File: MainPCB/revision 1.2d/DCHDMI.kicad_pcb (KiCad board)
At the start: 2 copper layers, 66.6 x 51.3 mm, 235 parts, among them CON1 3-1775333-2, CON2 2001-1-2-21-00-BK, CON3 CONN_01X06, CON4 CONN_01X03, U1 MCP1826S-1202E/DB, U2 MIC5219-2.5YM5-TR, U3 LP5907MFX-1.8/NOPB, U4 ADV7513, U5 664G-03LF, U6 10CL025, U7 MX25L1606EM1I-12G, U8 ESP-12E

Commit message: Added 1.2d
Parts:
- removed the ? at (133.8, 117.0)
- removed the ? at (133.8, 115.2)
- added ?: , pads:via-3mm, F.Cu at (140.9, 106.2)
- added ?: , pads:via-3mm, F.Cu at (148.6, 89.3)
- added ?: , pads:via-3mm, F.Cu at (186.4, 91.8)
- added ?: , pads:via-3mm, F.Cu at (186.4, 90.2)
- added ?: , pads:via-3mm, F.Cu at (186.4, 88.6)
- added ?: , pads:via-3mm, F.Cu at (169.1, 96.2)
- added ?: , pads:via-3mm, F.Cu at (169.1, 95.0)
- added ?: , pads:via-3mm, F.Cu at (169.2, 91.9)
- added ?: , pads:via-3mm, F.Cu at (169.1, 93.8)
- added ?: , pads:via-3mm, F.Cu at (158.2, 91.9)
- added ?: , pads:via-3mm, F.Cu at (160.4, 91.9)
- added ?: , pads:via-3mm, F.Cu at (136.0, 116.0)
- added ?: , pads:via-3mm, F.Cu at (155.8, 101.0)
- added ?: , pads:.6Cast, F.Cu at (168.3, 109.4)
- added ?: , pads:via-3mm, F.Cu at (153.2, 98.8)
- added ?: , pads:via-3mm, F.Cu at (154.2, 118.7)
- added ?: , pads:via-3mm, F.Cu at (158.4, 123.8)
- added ?: , pads:via-3mm, F.Cu at (161.4, 112.1)
- added ?: , pads:via-3mm, F.Cu at (160.2, 112.2)
- added ?: , pads:via-3mm, F.Cu at (163.4, 121.6)
- added ?: , pads:via-3mm, F.Cu at (160.8, 121.7)
- added ?: , pads:via-3mm, F.Cu at (158.7, 121.7)
- added ?: , pads:via-3mm, F.Cu at (146.2, 121.7)
- added ?: , pads:via-3mm, F.Cu at (135.3, 114.9)
- added ?: , pads:via-3mm, F.Cu at (148.1, 111.0)
- added ?: , pads:via-3mm, F.Cu at (149.6, 111.0)
- added ?: , pads:via-3mm, F.Cu at (152.9, 118.7)
- added ?: , pads:.6Cast, F.Cu at (184.7, 123.4)
- added ?: , pads:.6Cast, F.Cu at (184.7, 121.4)
- added ?: , pads:.6Cast, F.Cu at (184.7, 119.4)
- added ?: , pads:.6Cast, F.Cu at (184.7, 117.4)
- added ?: , pads:.6Cast, F.Cu at (184.7, 115.4)
- added ?: , pads:.6Cast, F.Cu at (184.7, 113.4)
- added ?: , pads:.6Cast, F.Cu at (184.7, 111.4)
- added ?: , pads:via-3mm, F.Cu at (141.6, 107.8)
- added ?: , pads:.6Cast, F.Cu at (184.7, 109.4)
- added ?: , pads:.6Cast, F.Cu at (168.3, 123.4)
- added ?: , pads:.6Cast, F.Cu at (168.3, 121.4)
- added ?: , pads:.6Cast, F.Cu at (168.3, 119.4)
- added ?: , pads:.6Cast, F.Cu at (168.3, 117.4)
- added ?: , pads:.6Cast, F.Cu at (168.3, 115.4)
- added ?: , pads:.6Cast, F.Cu at (168.3, 113.4)
- added ?: , pads:.6Cast, F.Cu at (168.3, 111.4)
- added ?: , pads:via-3mm, F.Cu at (186.4, 101.2)
- added ?: , pads:via-3mm, F.Cu at (184.3, 101.2)
- added ?: , pads:via-3mm, F.Cu at (141.9, 111.5)
- added ?: , pads:via-3mm, F.Cu at (184.6, 103.5)
- added ?: , pads:via-3mm, F.Cu at (144.2, 111.0)
- added ?: , pads:via-3mm, F.Cu at (144.6, 89.5)
- added ?: , pads:via-3mm, F.Cu at (146.8, 87.0)
- added ?: , pads:via-3mm, F.Cu at (148.7, 87.0)
- added C41: 47p, Capacitors_SMD:C_0603_HandSoldering, F.Cu at (185.3, 97.0)
- added C46: 47p, Capacitors_SMD:C_0603_HandSoldering, F.Cu at (185.3, 98.5)
- added C47: 47p, Capacitors_SMD:C_0603_HandSoldering, F.Cu at (185.3, 100.0)
- added C48: .1u, Capacitors_SMD:C_0603_HandSoldering, F.Cu at (180.9, 105.2)
- added C49: 22u, Capacitors_SMD:C_0603_HandSoldering, F.Cu at (179.4, 105.2)
- added R18: 10K, Capacitors_SMD:C_0603_HandSoldering, F.Cu at (143.9, 120.6)
- added R19: 10K, Capacitors_SMD:C_0603_HandSoldering, F.Cu at (136.6, 120.4)
- added R20: 10K, Capacitors_SMD:C_0603_HandSoldering, F.Cu at (149.9, 118.2)
- added R7: 10K, Capacitors_SMD:C_0603_HandSoldering, F.Cu at (133.8, 116.3)
- ?: renamed from CON3; value CONN_01X06 -> (none)
- ?: renamed from CON4; value CONN_01X03 -> (none)
- JP1: value Jumper_NO_Small -> (none)
- moved C8 0.21 mm to (151.8, 116.8)
- moved C9 0.21 mm to (155.4, 116.8)
- moved ? 0.09 mm to (164.8, 109.8)
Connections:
- U6 pad 145: (no net) -> GND
- U6 pad 21: GND -> /nCE
- U6 pad 9: +3V3 -> Net-(R7-Pad2)
- U8 pad 13: Net-(U8-Pad13) -> /nCE
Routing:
- net GND: track 204.5 -> 272.5 mm, vias 3 -> 2
- net /nCE: track 0.00 -> 34.8 mm, vias 0 -> 1
- net +3V3: track 389.6 -> 406.5 mm, vias 24 -> 27
- net Net-(R7-Pad2): track 0.00 -> 13.6 mm
- net /ABCK: track 67.4 -> 73.5 mm
- net /ADAT: track 66.5 -> 71.9 mm
- net /TDI: track 12.2 -> 16.9 mm
- net /ALRK: track 70.1 -> 73.5 mm
- net /TMS: track 9.11 -> 10.4 mm
- net /TDO: track 8.45 -> 9.34 mm
- net /TCK: track 9.73 -> 10.6 mm
- net /MOSI: track 71.3 -> 71.6 mm, vias 3 -> 2
- net /MISO: track 70.1 -> 70.3 mm, vias 3 -> 2
- net Net-(R14-Pad1): track 49.0 -> 49.2 mm, vias 2 -> 1
- net /DCLK: track 74.4 -> 74.6 mm, vias 3 -> 2
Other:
- board text added: "@chriz2600"
- board text added: "@citrus3000psi"
- board text added: "DCHDMI 1.2d"
- board text added: "P1"
- board text added: "P2"
- board text removed: "@citrus3000psi @chriz2600"
- board text removed: "DCHDMI 1.2a"
- board text removed: "PAD"
- board text removed: "RX"
- board text removed: "TX"

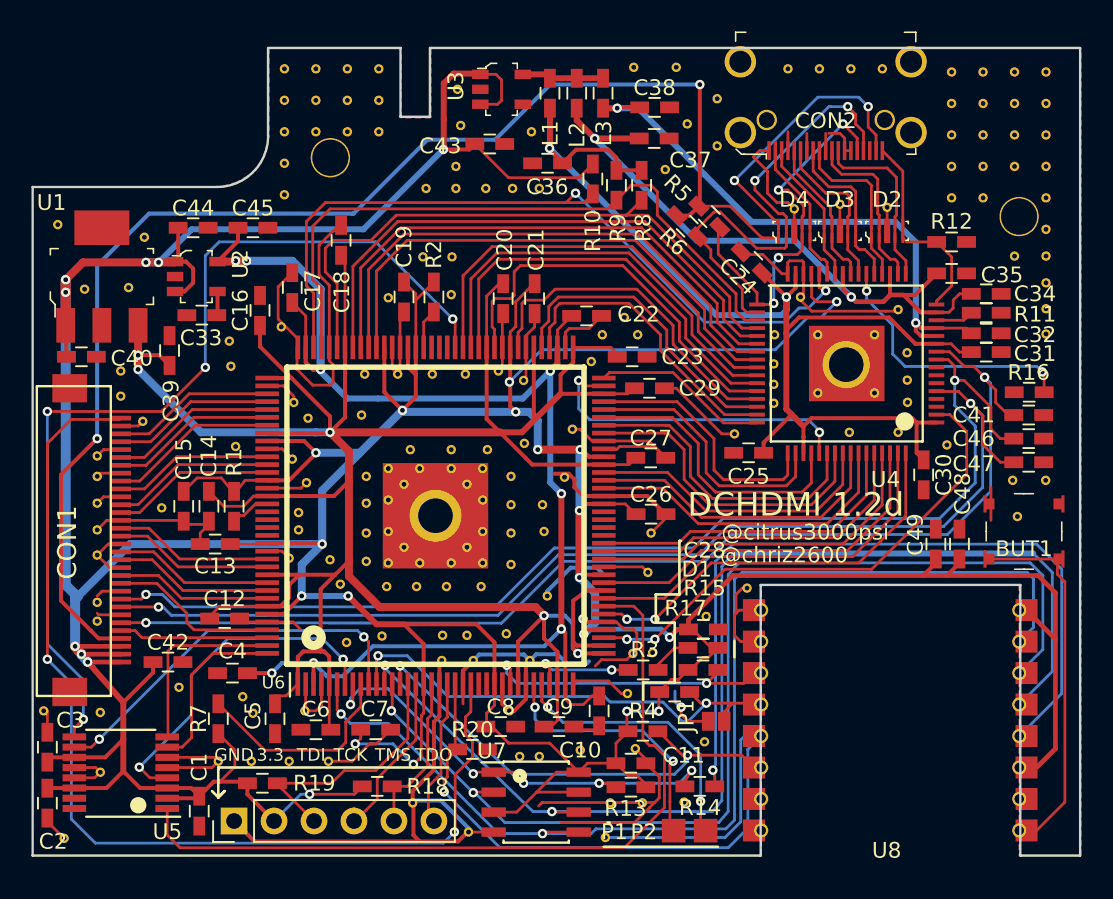
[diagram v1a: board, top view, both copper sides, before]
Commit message: 4 layer version
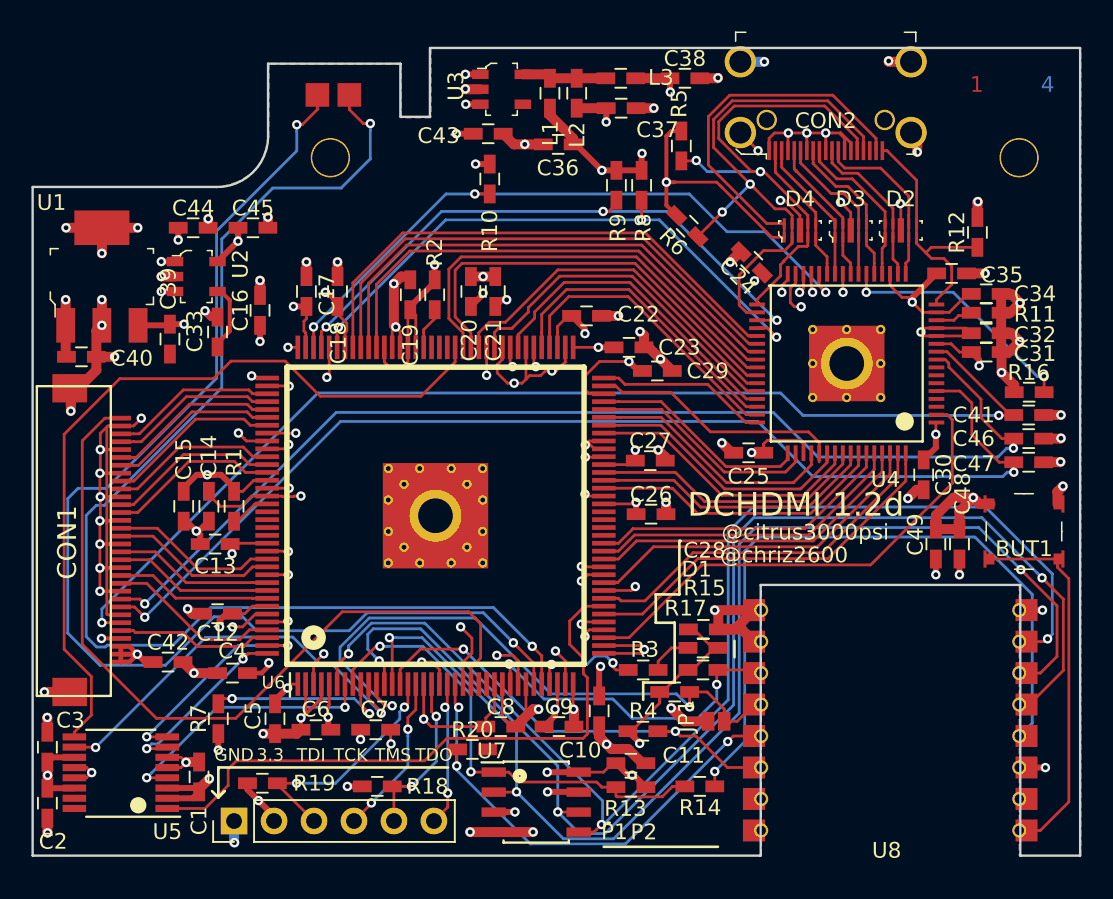
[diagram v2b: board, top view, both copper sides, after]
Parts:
- removed the ? at (140.9, 106.2)
- removed the ? at (148.6, 89.3)
- removed the ? at (124.0, 123.9)
- removed the ? at (139.3, 115.8)
- removed the ? at (170.4, 83.9)
- removed the ? at (173.3, 83.6)
- removed the ? at (176.3, 83.8)
- removed the ? at (167.4, 108.0)
- removed the ? at (166.6, 98.2)
- removed the ? at (170.8, 89.5)
- removed the ? at (180.1, 98.9)
- removed the ? at (131.3, 114.3)
- removed the ? at (186.4, 91.8)
- removed the ? at (126.3, 119.7)
- removed the ? at (145.2, 94.4)
- removed the ? at (151.6, 94.2)
- removed the ? at (129.1, 85.7)
- removed the ? at (123.6, 84.9)
- removed the ? at (125.3, 89.0)
- removed the ? at (128.1, 88.9)
- removed the ? at (127.6, 94.2)
- removed the ? at (127.6, 95.8)
- removed the ? at (137.8, 91.4)
- removed the ? at (186.4, 90.2)
- removed the ? at (134.6, 93.9)
- removed the ? at (134.5, 92.3)
- removed the ? at (153.7, 79.0)
- removed the ? at (148.9, 81.2)
- removed the ? at (147.0, 82.6)
- removed the ? at (148.9, 82.6)
- removed the ? at (150.8, 82.6)
- removed the ? at (152.5, 82.6)
- removed the ? at (154.2, 82.6)
- removed the ? at (152.3, 115.8)
- removed the ? at (186.4, 88.6)
- removed the ? at (159.8, 114.7)
- removed the ? at (164.7, 117.8)
- removed the ? at (130.2, 102.9)
- removed the ? at (134.9, 99.0)
- removed the ? at (129.0, 97.4)
- removed the ? at (126.1, 99.6)
- removed the ? at (126.1, 100.9)
- removed the ? at (126.1, 102.6)
- removed the ? at (126.1, 104.3)
- removed the ? at (126.1, 105.9)
- removed the ? at (169.1, 96.2)
- removed the ? at (126.1, 108.9)
- removed the ? at (126.1, 110.1)
- removed the ? at (138.3, 119.0)
- removed the ? at (140.8, 119.0)
- removed the ? at (135.9, 119.0)
- removed the ? at (133.8, 119.0)
- removed the ? at (152.1, 110.9)
- removed the ? at (153.6, 112.6)
- removed the ? at (150.0, 112.6)
- removed the ? at (148.0, 112.6)
- removed the ? at (169.1, 95.0)
- removed the ? at (159.6, 90.8)
- removed the ? at (157.5, 93.6)
- removed the ? at (156.3, 97.9)
- removed the ? at (154.5, 104.4)
- removed the ? at (154.4, 102.7)
- removed the ? at (146.0, 99.2)
- removed the ? at (148.6, 99.2)
- removed the ? at (150.9, 99.2)
- removed the ? at (152.4, 100.9)
- removed the ? at (152.4, 102.7)
- removed the ? at (169.2, 91.9)
- removed the ? at (152.4, 104.5)
- removed the ? at (152.4, 106.5)
- removed the ? at (150.5, 107.9)
- removed the ? at (148.3, 107.9)
- removed the ? at (146.4, 107.9)
- removed the ? at (144.5, 107.9)
- removed the ? at (143.2, 106.3)
- removed the ? at (143.2, 104.5)
- removed the ? at (143.2, 102.6)
- removed the ? at (143.2, 100.9)
- removed the ? at (169.1, 93.8)
- removed the ? at (138.9, 104.3)
- removed the ? at (138.9, 103.2)
- removed the ? at (139.4, 101.3)
- removed the ? at (138.5, 99.8)
- removed the ? at (139.5, 97.2)
- removed the ? at (138.6, 96.2)
- removed the ? at (142.9, 97.0)
- removed the ? at (143.1, 94.4)
- removed the ? at (149.5, 94.4)
- removed the ? at (147.4, 94.4)
- removed the ? at (158.2, 91.9)
- removed the ? at (186.4, 83.2)
- removed the ? at (182.4, 83.2)
- removed the ? at (180.4, 83.2)
- removed the ? at (186.4, 81.2)
- removed the ? at (184.4, 81.2)
- removed the ? at (182.4, 81.2)
- removed the ? at (180.4, 81.2)
- removed the ? at (186.4, 79.2)
- removed the ? at (184.4, 79.2)
- removed the ? at (182.4, 79.2)
- removed the ? at (160.4, 91.9)
- removed the ? at (180.4, 79.2)
- removed the ? at (186.4, 77.2)
- removed the ? at (184.4, 77.2)
- removed the ? at (182.4, 77.2)
- removed the ? at (180.4, 77.2)
- removed the ? at (186.4, 75.2)
- removed the ? at (184.4, 75.2)
- removed the ? at (182.4, 75.2)
- removed the ? at (186.4, 86.9)
- removed the ? at (186.4, 85.2)
- removed the ? at (136.0, 116.0)
- removed the ? at (155.8, 101.0)
- removed the ? at (184.4, 86.9)
- removed the ? at (180.4, 75.2)
- removed the ? at (153.2, 98.8)
- removed the ? at (154.2, 118.7)
- removed the ? at (158.4, 123.8)
- removed the ? at (161.4, 112.1)
- removed the ? at (160.2, 112.2)
- removed the ? at (163.4, 121.6)
- removed the ? at (160.8, 121.7)
- removed the ? at (158.7, 121.7)
- removed the ? at (146.2, 121.7)
- removed the ? at (135.3, 114.9)
- removed the ? at (148.1, 111.0)
- removed the ? at (149.6, 111.0)
- removed the ? at (152.9, 118.7)
- removed the ? at (141.6, 107.8)
- removed the ? at (186.4, 101.2)
- removed the ? at (184.3, 101.2)
- removed the ? at (141.9, 111.5)
- removed the ? at (184.6, 103.5)
- removed the ? at (164.8, 109.8)
- removed the ? at (177.6, 96.2)
- removed the ? at (177.6, 94.8)
- removed the ? at (177.6, 93.0)
- removed the ? at (138.0, 83.0)
- removed the ? at (138.0, 81.0)
- removed the ? at (138.0, 79.0)
- removed the ? at (140.0, 79.0)
- removed the ? at (144.2, 111.0)
- removed the ? at (142.0, 79.0)
- removed the ? at (144.0, 79.0)
- removed the ? at (144.0, 77.0)
- removed the ? at (142.0, 77.0)
- removed the ? at (140.0, 77.0)
- removed the ? at (138.0, 77.0)
- removed the ? at (144.0, 75.0)
- removed the ? at (142.0, 75.0)
- removed the ? at (140.0, 75.0)
- removed the ? at (138.0, 75.0)
- removed the ? at (144.6, 89.5)
- removed the ? at (170.0, 75.0)
- removed the ? at (172.0, 75.0)
- removed the ? at (176.0, 75.0)
- removed the ? at (174.0, 75.0)
- removed the ? at (171.9, 91.9)
- removed the ? at (171.9, 95.6)
- removed the ? at (175.5, 95.6)
- removed the ? at (175.5, 91.9)
- removed the ? at (173.7, 93.8)
- removed the ? at (163.6, 78.5)
- removed the ? at (146.8, 87.0)
- removed the ? at (162.2, 81.4)
- removed the ? at (165.5, 79.9)
- removed the ? at (165.5, 76.9)
- removed the ? at (162.9, 74.9)
- removed the ? at (160.2, 74.9)
- removed the ? at (149.7, 123.5)
- removed the ? at (177.0, 90.3)
- removed the ? at (173.9, 98.1)
- removed the ? at (177.0, 98.1)
- removed the ? at (153.2, 94.8)
- removed the ? at (148.7, 87.0)
- removed the ? at (156.8, 118.3)
- removed the ? at (160.3, 118.2)
- removed the ? at (149.2, 78.6)
- removed the ? at (149.0, 76.3)
- removed the ? at (161.3, 104.5)
- removed the ? at (161.1, 107.0)
- removed the ? at (154.7, 108.5)
- removed the ? at (138.3, 106.1)
- removed the ? at (126.6, 115.9)
- removed the ? at (122.7, 115.8)
- moved ? 52.0 mm to (142.1, 75.1)
- moved R10 6.55 mm to (151.1, 82.0)
- moved R5 4.84 mm to (163.2, 79.9), turned to 270 degrees
- moved C18 3.26 mm to (141.4, 89.2)
- moved C37 2.85 mm to (159.4, 77.5)
- moved C38 2.67 mm to (163.4, 75.6)
- moved C21 2.54 mm to (151.4, 89.2), turned to 90 degrees
- moved C1 2.17 mm to (132.6, 120.0), turned to 90 degrees
- moved C20 2.10 mm to (149.8, 89.2), turned to 90 degrees
- moved R12 1.75 mm to (182.0, 85.4), turned to 90 degrees
- moved L3 1.47 mm to (159.4, 75.6), turned to 180 degrees
- moved C33 1.47 mm to (133.8, 91.7), turned to 270 degrees
- moved C36 1.38 mm to (155.4, 79.8)
- moved C29 1.21 mm to (161.7, 94.2)
- moved C17 0.93 mm to (139.4, 89.2)
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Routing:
- net /PAD2: track 17.5 -> 78.9 mm
- net /PAD1: track 16.7 -> 77.3 mm
- net GND: track 272.5 -> 241.3 mm, vias 2 -> 93
- net /+5: track 104.0 -> 127.8 mm, vias 4 -> 2
- net +3V3: track 406.5 -> 390.4 mm, vias 27 -> 37
- net +2.5: track 88.0 -> 103.0 mm, vias 8 -> 7
- net /VCLK: track 65.3 -> 50.5 mm, vias 2 -> 0
- net /X1: track 50.4 -> 39.5 mm
- net /CLK: track 60.1 -> 49.9 mm, vias 4 -> 0
- net /ESP_SCL: track 30.7 -> 39.4 mm
- net /SCL_H: track 24.5 -> 32.3 mm, vias 4 -> 2
- net /INT: track 49.4 -> 42.2 mm, vias 2 -> 3
- net /MOSI: track 71.6 -> 78.5 mm, vias 2 -> 3
- net /DCLK: track 74.6 -> 81.3 mm, vias 2 -> 3
- net /MISO: track 70.3 -> 76.6 mm, vias 2 -> 3
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- added copper zone on In1.Cu, net GND
- added copper zone on In2.Cu, net GND
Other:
- outline, holes or cut-outs redrawn
- copper layers 2 -> 4
- board text added: "1"
- board text added: "2"
- board text added: "3"
- board text added: "4"
